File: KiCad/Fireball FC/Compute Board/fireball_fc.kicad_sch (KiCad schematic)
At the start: 33 parts, among them J1 Conn_01x04, J2 Conn_01x03, J3 Conn_01x04, J4 Conn_01x09, J5 Conn_01x06, SW1 HX 3X4X2-2P-2.5N-04, U1 RP2040, U4 CAT24C256WI-GT3, U7 W25Q16JVUXIQ, X1 12MHZ Crystal

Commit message: finish compute, still needs cleanup
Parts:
- removed C21: 0.1uF, Capacitor_SMD:C_0402_1005Metric, symbol Device:C_Small
- removed C22: 10uF, Capacitor_SMD:C_0805_2012Metric, symbol Device:C_Small
- removed Card1: HYC77-TF09-200, lcsc_footprints:C341092_TF-SMD_HYC77-TF09-200, symbol lcsc_imported:HYC77-TF09-200
- removed J5: Conn_01x06, Connector_PinHeader_2.00mm:PinHeader_1x06_P2.00mm_Vertical, symbol Connector_Generic:Conn_01x06
- added J5: Conn_01x07, Connector_PinSocket_2.00mm:PinSocket_1x07_P2.00mm_Vertical, symbol Connector_Generic:Conn_01x07
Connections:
- net +3V3: now also J5.2 (Pin_2)
- net +5V: now also J5.3 (Pin_3)
- net 5V_EN: now also U1.3 (GPIO1), J5.7 (Pin_7); no longer U1.32 (GPIO21)
- net BUZZER: now also J5.6 (Pin_6)
- net GND: now also J5.1 (Pin_1)
- net NEOPIXEL: now also U1.37 (GPIO25); no longer U1.17 (GPIO14)
- net SCL: now also J5.5 (Pin_5)
- net SDA: now also J5.4 (Pin_4)
- net SDLED: no longer names the net of U1.27 (GPIO16)
- net SD_CS: no longer names the net of U1.7 (GPIO5)
- no-connect marks 11 -> 8
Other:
- note removed: "---->"
- note removed: "I think this is Card Detection. I left it as NC"
- note removed: "SD"

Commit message: waow
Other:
- moved on the sheet: C19, D7, J2, J3, J5, R4, U7

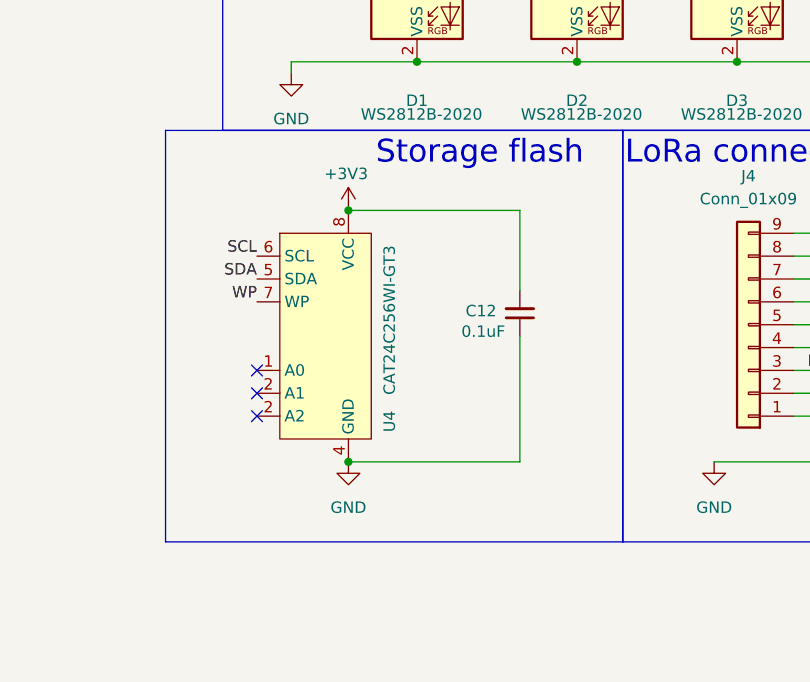
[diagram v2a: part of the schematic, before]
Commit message: add 24LC512
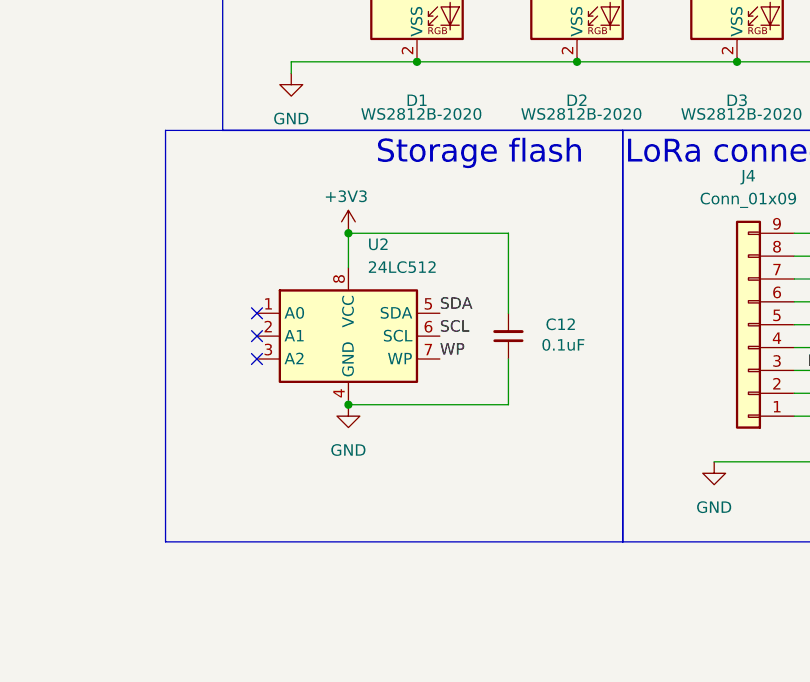
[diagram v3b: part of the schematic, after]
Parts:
- removed U4: CAT24C256WI-GT3, Package_SO:SOIC-8-1EP_3.9x4.9mm_P1.27mm_EP2.29x3mm, symbol fireball:MB85RC256VPF
- added U2: 24LC512, Package_SO:SOIC-8-1EP_3.9x4.9mm_P1.27mm_EP2.29x3mm, symbol Memory_EEPROM:24LC512
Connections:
- net +3V3: now also U2.8 (VCC)
- net GND: now also U2.4 (GND)
- net SCL: now also U2.6 (SCL)
- net SDA: now also U2.5 (SDA)
- net WP: now also U2.7 (WP)
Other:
- moved on the sheet: C12
